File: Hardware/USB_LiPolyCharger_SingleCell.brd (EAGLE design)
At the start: 35.6 x 38.1 mm, 27 parts, among them J1 POWER_JACKSMD, U1 MCP73831, X1 USBSMD

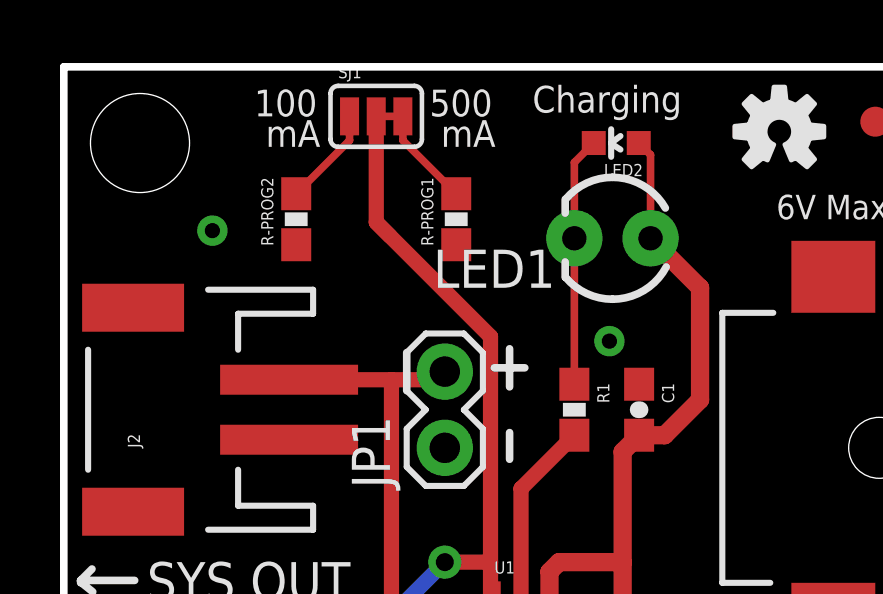
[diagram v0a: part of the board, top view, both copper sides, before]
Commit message: Fixed Airwire
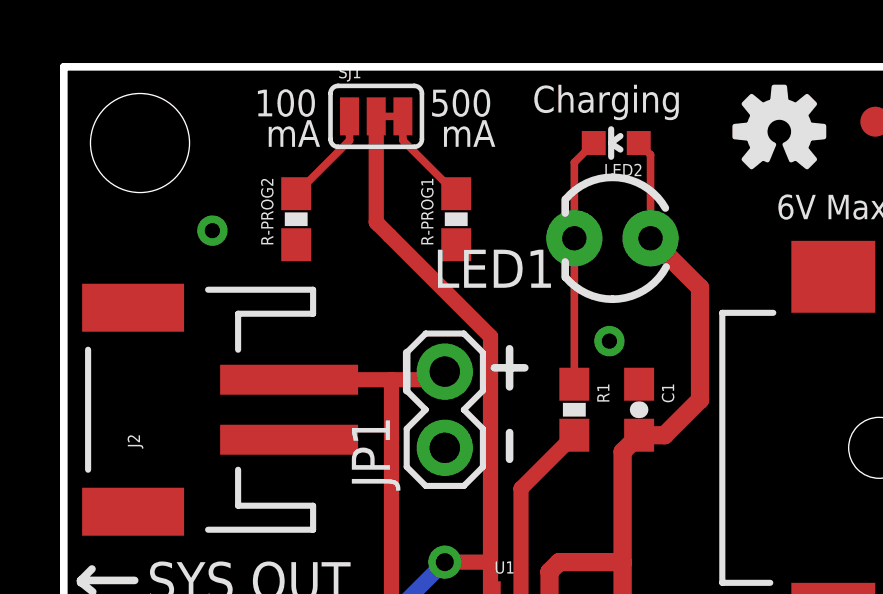
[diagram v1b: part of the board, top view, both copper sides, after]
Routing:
- net PROG: track 24.9 -> 24.4 mm
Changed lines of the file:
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@@
 <layer number="18" name="Vias" color="2" fill="1" visible="yes" active="yes"/>
 <layer number="19" name="Unrouted" color="6" fill="1" visible="yes" active="yes"/>
-<layer number="20" name="Dimension" color="24" fill="1" visible="yes" active="yes"/>
+<layer number="20" name="Dimension" color="15" fill="1" visible="yes" active="yes"/>
 <layer number="21" name="tPlace" color="16" fill="1" visible="yes" active="yes"/>
 <layer number="22" name="bPlace" color="14" fill="1" visible="yes" active="yes"/>
@@
 <layer number="47" name="Measures" color="7" fill="1" visible="no" active="yes"/>
 <layer number="48" name="Document" color="7" fill="1" visible="no" active="yes"/>
-<layer number="49" name="Reference" color="7" fill="1" visible="yes" active="yes"/>
+<layer number="49" name="Reference" color="7" fill="1" visible="no" active="yes"/>
 <layer number="50" name="dxf" color="7" fill="1" visible="no" active="yes"/>
 <layer number="51" name="tDocu" color="6" fill="1" visible="yes" active="yes"/>
@@
 <contactref element="SJ1" pad="2"/>
 <wire x1="9.144" y1="36.449" x2="9.144" y2="32.9184" width="0.508" layer="1"/>
-<wire x1="9.144" y1="32.9184" x2="9.6012" y2="32.4612" width="0.508" layer="1"/>
+<wire x1="9.144" y1="32.9184" x2="9.2202" y2="32.8422" width="0.508" layer="1"/>
 <contactref element="U1" pad="5"/>
+<wire x1="9.2202" y1="32.8422" x2="9.6012" y2="32.4612" width="0.508" layer="1"/>
 <wire x1="12.954" y1="20.4161" x2="13.02" y2="20.3501" width="0.508" layer="1"/>
 <wire x1="12.954" y1="20.4161" x2="12.954" y2="21.59" width="0.508" layer="1"/>
 <wire x1="12.954" y1="21.59" x2="12.954" y2="29.1084" width="0.508" layer="1"/>
-<wire x1="12.954" y1="29.1084" x2="9.2202" y2="32.8422" width="0.508" layer="1"/>
+<wire x1="12.954" y1="29.1084" x2="9.6012" y2="32.4612" width="0.508" layer="1"/>
 <contactref element="PROG" pad="P$2"/>
 <wire x1="7.747" y1="18.0594" x2="7.8994" y2="18.0594" width="0.508" layer="16"/>
@@
 <via x="11.43" y="21.59" extent="1-16" drill="0.6"/>
 <wire x1="11.43" y1="21.59" x2="12.954" y2="21.59" width="0.508" layer="1"/>
-<wire x1="9.2202" y1="32.8422" x2="9.144" y2="32.9184" width="0" layer="19" extent="1-1"/>
 </signal>
 <signal name="N$4">
